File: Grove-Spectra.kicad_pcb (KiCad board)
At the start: 2 copper layers, 42.3 x 24.6 mm, 24 parts, among them IC1 PCA9536DP,118, IC2 AS7341-DLGT, IC3 SPX3819M5-L-1-8_TR, J1 114020164, J2 Conn_01x02, Q1 BS250FTA, Q2 BS250FTA, Q3 BS250FTA

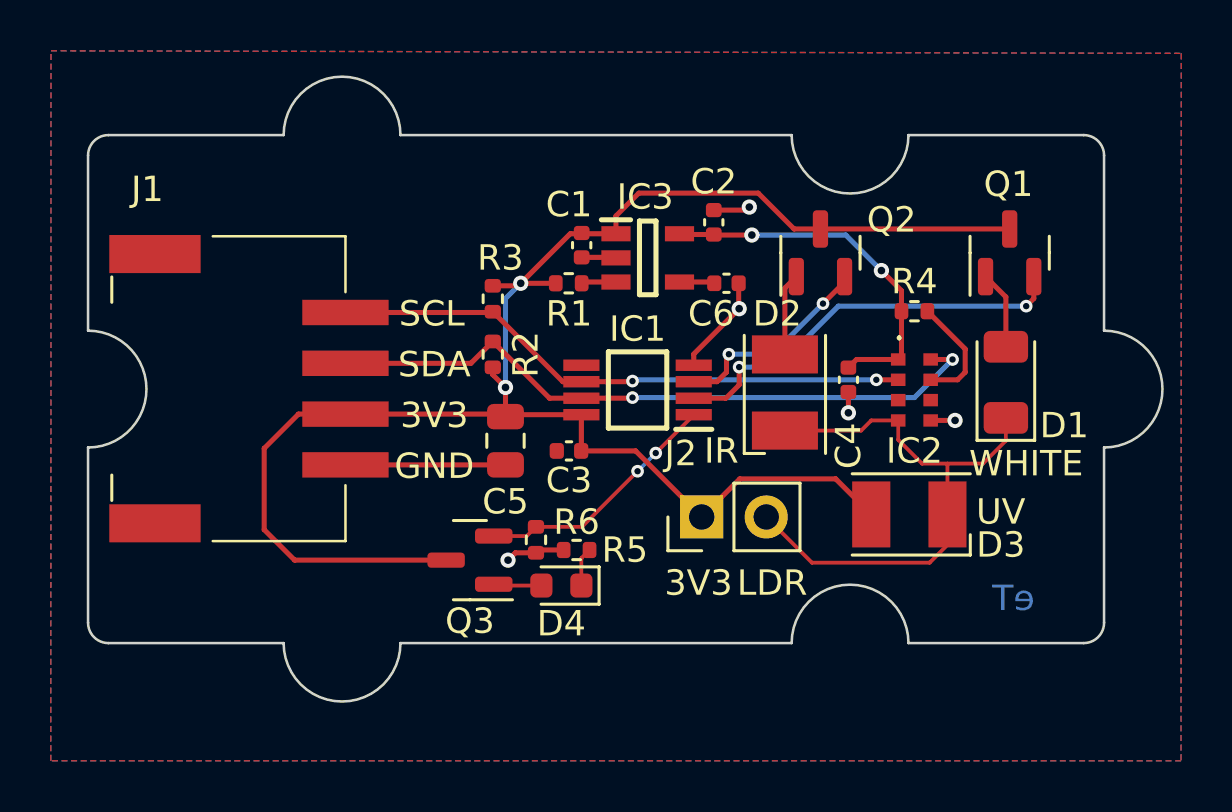
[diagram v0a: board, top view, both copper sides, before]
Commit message: Updated for DFA
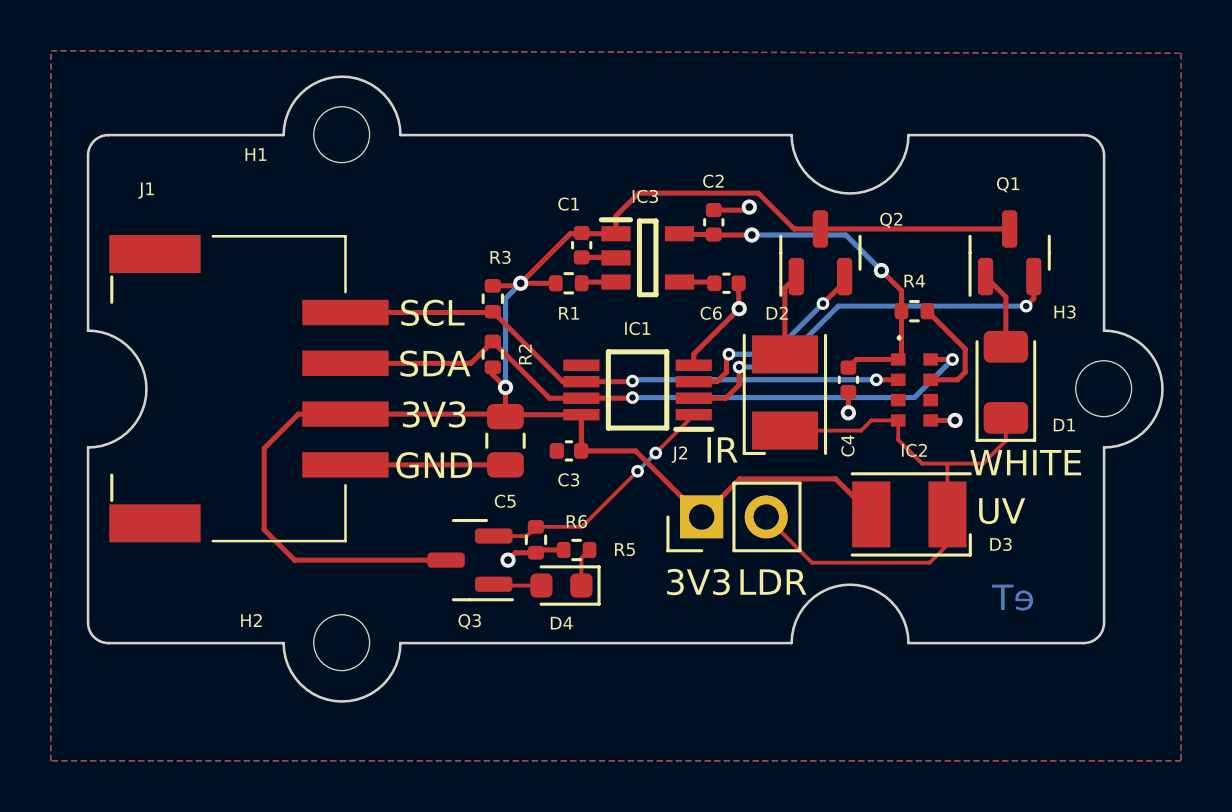
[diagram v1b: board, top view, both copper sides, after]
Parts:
- added FID1: Fiducial, personal:Product Stamp, B.Cu at (170.7, 90.0)
- added H1: MountingHole, MountingHole:MountingHole_2.2mm_M2, F.Cu at (130.2, 78.5)
- added H2: MountingHole, MountingHole:MountingHole_2.2mm_M2, F.Cu at (130.2, 98.5)
- added H3: MountingHole, MountingHole:MountingHole_2.2mm_M2, F.Cu at (160.2, 88.5)

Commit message: Fixed for DA
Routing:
- net /LDR: track 22.7 -> 21.5 mm
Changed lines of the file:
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@@
   (title_block
     (title "Grove-Spectra")
-    (date "2022-11-22")
+    (date "2022-11-23")
     (rev "A")
   )
@@
       (sketchpadsonfab false)
       (subtractmaskfromsilk false)
-      (outputformat 1)
+      (outputformat 4)
       (mirror false)
       (drillshape 0)
@@
   (segment (start 148.0625 82.2625) (end 146.650489 80.850489) (width 0.2) (layer "F.Cu") (net 1))
   (segment (start 139.68 91) (end 141.825 91) (width 0.2) (layer "F.Cu") (net 1))
-  (segment (start 139.688 90.992) (end 139.68 91) (width 0.2) (layer "F.Cu") (net 1))
   (segment (start 130.4 89.55) (end 128.55 89.55) (width 0.2) (layer "F.Cu") (net 1))
   (segment (start 139.688 89.575) (end 139.688 90.992) (width 0.2) (layer "F.Cu") (net 1))
@@
   (segment (start 141.825 91) (end 144.425 93.6) (width 0.2) (layer "F.Cu") (net 1))
   (segment (start 130.4 89.55) (end 136.6 89.55) (width 0.2) (layer "F.Cu") (net 1))
-  (segment (start 136.775 89.575) (end 136.7 89.65) (width 0.2) (layer "F.Cu") (net 1))
   (segment (start 149.1 82.2625) (end 156.55 82.2625) (width 0.2) (layer "F.Cu") (net 1))
   (segment (start 146.650489 80.850489) (end 141.949511 80.850489) (width 0.2) (layer "F.Cu") (net 1))
@@
   (segment (start 139.25 82.45) (end 141.05 82.45) (width 0.2) (layer "F.Cu") (net 1))
   (segment (start 137.3 84.4) (end 138.68 84.4) (width 0.2) (layer "F.Cu") (net 1))
-  (segment (start 136.6 89.55) (end 136.7 89.65) (width 0.2) (layer "F.Cu") (net 1))
   (segment (start 136.2 87.71) (end 136.2 88) (width 0.2) (layer "F.Cu") (net 1))
   (segment (start 141.949511 80.850489) (end 141.05 81.75) (width 0.2) (layer "F.Cu") (net 1))
-  (segment (start 136.7 89.65) (end 136.85 89.65) (width 0.2) (layer "F.Cu") (net 1))
   (via (at 137.3 84.4) (size 0.6) (drill 0.3) (layers "F.Cu" "B.Cu") (net 1))
   (via (at 136.7 88.5) (size 0.6) (drill 0.3) (layers "F.Cu" "B.Cu") (net 1))
@@
   (segment (start 136.7 85) (end 137.3 84.4) (width 0.2) (layer "B.Cu") (net 1))
   (segment (start 146.18 81.52) (end 146.3 81.4) (width 0.2) (layer "F.Cu") (net 2))
-  (segment (start 138.01 94.9) (end 137.9 95.01) (width 0.2) (layer "F.Cu") (net 2))
   (segment (start 138.99 94.9) (end 138.01 94.9) (width 0.2) (layer "F.Cu") (net 2))
   (segment (start 130.4 91.55) (end 136.7 91.55) (width 0.2) (layer "F.Cu") (net 2))
-  (segment (start 136.6 91.65) (end 136.7 91.55) (width 0.2) (layer "F.Cu") (net 2))
   (segment (start 139.7 83.38) (end 141.03 83.38) (width 0.2) (layer "F.Cu") (net 2))
   (segment (start 145.88 84.4) (end 145.88 85.38) (width 0.2) (layer "F.Cu") (net 2))
   (segment (start 144.112 87.188) (end 145.9 85.4) (width 0.2) (layer "F.Cu") (net 2))
   (segment (start 144.9 81.52) (end 146.18 81.52) (width 0.2) (layer "F.Cu") (net 2))
-  (segment (start 141.03 83.38) (end 141.05 83.4) (width 0.2) (layer "F.Cu") (net 2))
   (segment (start 153.438 89.8) (end 154.4 89.8) (width 0.2) (layer "F.Cu") (net 2))
   (segment (start 145.88 85.38) (end 145.9 85.4) (width 0.2) (layer "F.Cu") (net 2))
@@
   (via (at 150.2 89.5) (size 0.6) (drill 0.3) (layers "F.Cu" "B.Cu") (net 2))
   (segment (start 150.52 87.4) (end 152.162 87.4) (width 0.2) (layer "F.Cu") (net 3))
-  (segment (start 152.29 87.272) (end 152.162 87.4) (width 0.2) (layer "F.Cu") (net 3))
-  (segment (start 144.92 82.5) (end 144.9 82.48) (width 0.2) (layer "F.Cu") (net 3))
   (segment (start 150.2 87.72) (end 150.52 87.4) (width 0.2) (layer "F.Cu") (net 3))
   (segment (start 146.4 82.5) (end 144.92 82.5) (width 0.2) (layer "F.Cu") (net 3))
@@
   (segment (start 144.9 82.48) (end 143.58 82.48) (width 0.2) (layer "F.Cu") (net 3))
   (segment (start 152.29 85.5) (end 152.29 84.69) (width 0.2) (layer "F.Cu") (net 3))
-  (segment (start 143.58 82.48) (end 143.55 82.45) (width 0.2) (layer "F.Cu") (net 3))
   (segment (start 152.29 85.5) (end 152.29 87.272) (width 0.2) (layer "F.Cu") (net 3))
   (via (at 151.5 83.9) (size 0.6) (drill 0.3) (layers "F.Cu" "B.Cu") (net 3))
@@
   (segment (start 153.1 91.5) (end 154.1 91.5) (width 0.15) (layer "F.Cu") (net 4))
   (segment (start 152.162 90.562) (end 153.1 91.5) (width 0.15) (layer "F.Cu") (net 4))
-  (segment (start 154.1 93.5) (end 154.1 94.7) (width 0.15) (layer "F.Cu") (net 4))
   (segment (start 150.7 90.2) (end 147.7 90.2) (width 0.15) (layer "F.Cu") (net 4))
   (segment (start 156.4 90.6) (end 156.4 89.7) (width 0.15) (layer "F.Cu") (net 4))
@@
   (segment (start 136.2375 94.35) (end 137.54 94.35) (width 0.15) (layer "F.Cu") (net 7))
   (segment (start 137.54 94.35) (end 137.9 93.99) (width 0.15) (layer "F.Cu") (net 7))
-  (segment (start 144.112 89.575) (end 144.112 89.588) (width 0.15) (layer "F.Cu") (net 7))
   (via (at 142.6157 91.0843) (size 0.5) (drill 0.25) (layers "F.Cu" "B.Cu") (net 7))
   (via (at 141.9 91.8) (size 0.5) (drill 0.25) (layers "F.Cu" "B.Cu") (net 7))
@@
   (segment (start 147.406416 87.7) (end 145.9 87.7) (width 0.2) (layer "B.Cu") (net 8))
   (segment (start 157.2 85.3) (end 149.806416 85.3) (width 0.2) (layer "B.Cu") (net 8))
-  (segment (start 150.05 84.1375) (end 150.05 84.35) (width 0.2) (layer "F.Cu") (net 9))
   (segment (start 145.400489 87.899011) (end 145.400489 87.286594) (width 0.2) (layer "F.Cu") (net 9))
   (segment (start 144.112 88.275) (end 145.0245 88.275) (width 0.2) (layer "F.Cu") (net 9))
@@
   (via (at 149.2 85.2) (size 0.5) (drill 0.25) (layers "F.Cu" "B.Cu") (net 9))
   (via (at 145.494259 87.192824) (size 0.5) (drill 0.25) (layers "F.Cu" "B.Cu") (net 9))
-  (segment (start 147.8 86.6) (end 147.207176 87.192824) (width 0.2) (layer "B.Cu") (net 9))
-  (segment (start 149.2 85.2) (end 147.8 86.6) (width 0.2) (layer "B.Cu") (net 9))
+  (segment (start 147.207176 87.192824) (end 149.2 85.2) (width 0.2) (layer "B.Cu") (net 9))
   (segment (start 147.207176 87.192824) (end 145.494259 87.192824) (width 0.2) (layer "B.Cu") (net 9))
   (segment (start 136.2 85.52) (end 138.955 88.275) (width 0.2) (layer "F.Cu") (net 11))
   (segment (start 141.7 88.250497) (end 141.675497 88.275) (width 0.2) (layer "F.Cu") (net 11))
   (segment (start 152.162 88.2) (end 151.3 88.2) (width 0.2) (layer "F.Cu") (net 11))
-  (segment (start 136.2 85.52) (end 136.07 85.65) (width 0.2) (layer "F.Cu") (net 11))
   (segment (start 130.4 85.55) (end 136.17 85.55) (width 0.2) (layer "F.Cu") (net 11))
   (segment (start 138.955 88.275) (end 139.688 88.275) (width 0.2) (layer "F.Cu") (net 11))
-  (segment (start 136.17 85.55) (end 136.2 85.52) (width 0.2) (layer "F.Cu") (net 11))
   (segment (start 141.675497 88.275) (end 139.688 88.275) (width 0.2) (layer "F.Cu") (net 11))
   (via (at 151.3 88.2) (size 0.5) (drill 0.25) (layers "F.Cu" "B.Cu") (net 11))
@@
   (segment (start 153.438 88.2) (end 154.5 88.2) (width 0.2) (layer "F.Cu") (net 14))
   (segment (start 141.05 84.35) (end 139.75 84.35) (width 0.2) (layer "F.Cu") (net 15))
-  (segment (start 139.75 84.35) (end 139.7 84.4) (width 0.2) (layer "F.Cu") (net 15))
-  (segment (start 144.87 84.35) (end 144.92 84.4) (width 0.2) (layer "F.Cu") (net 16))
   (segment (start 143.55 84.35) (end 144.87 84.35) (width 0.2) (layer "F.Cu") (net 16))
   (segment (start 139.6875 96.3) (end 139.6875 95.2225) (width 0.15) (layer "F.Cu") (net 19))
   (segment (start 139.6875 95.2225) (end 140.01 94.9) (width 0.15) (layer "F.Cu") (net 19))
   (segment (start 138.1125 96.3) (end 136.2875 96.3) (width 0.15) (layer "F.Cu") (net 20))
-  (segment (start 136.2875 96.3) (end 136.2375 96.25) (width 0.15) (layer "F.Cu") (net 20))
   (zone (net 2) (net_name "GND") (layers F&B.Cu) (hatch edge 0.508)
     (connect_pads thru_hole_only (clearance 0.15))
